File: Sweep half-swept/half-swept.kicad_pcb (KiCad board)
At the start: 2 copper layers, 109 x 86.9 mm, 25 parts, among them J2 AudioJack4dpb, SW1 SW_Push, SW10 SW_Push, SW11 SW_Push, SW12 SW_Push, SW13 SW_Push, SW14 SW_Push, SW15 SW_Push, SW16 SW_Push, SW17 SW_Push, SW2 SW_Push, SW3 SW_Push, SW4 SW_Push, SW5 SW_Push, SW6 SW_Push, SW7 SW_Push, SW8 SW_Push, SW9 SW_Push, U1 ProMicro-kbd

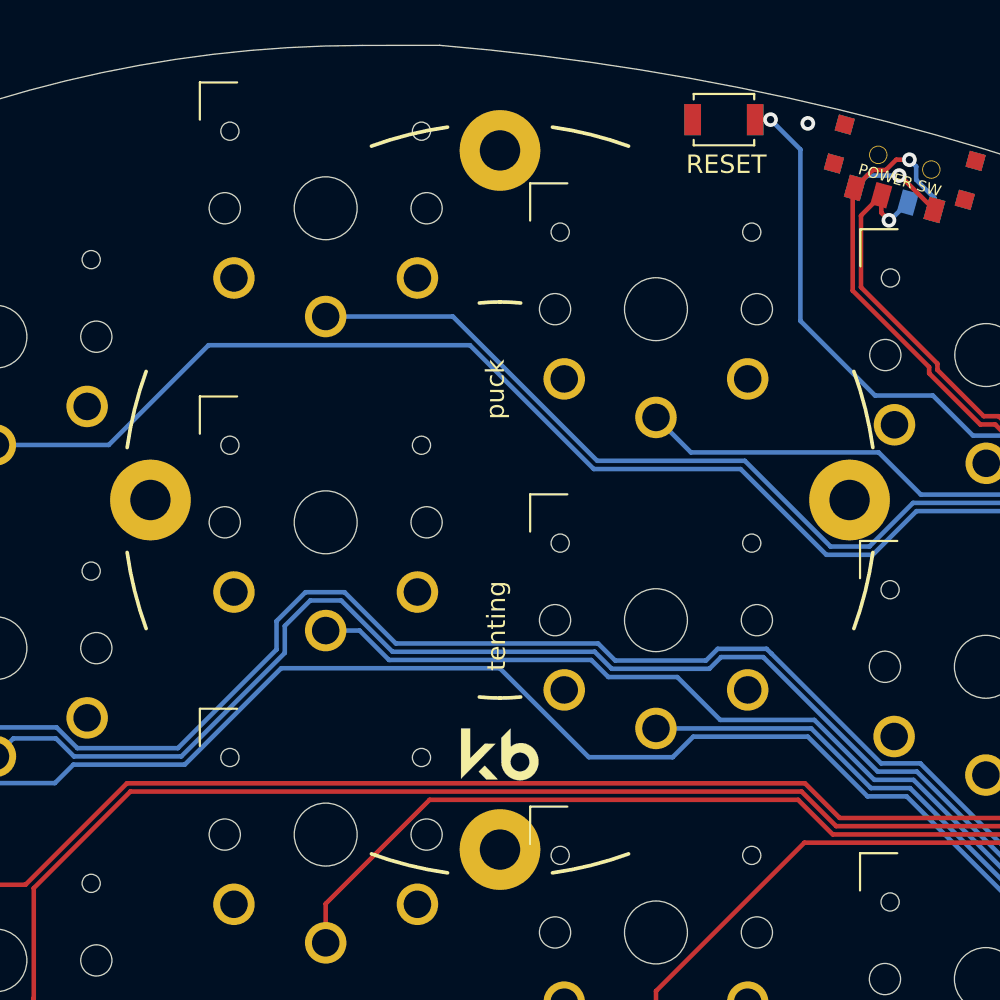
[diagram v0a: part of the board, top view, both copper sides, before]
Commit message: Remove tenting puck
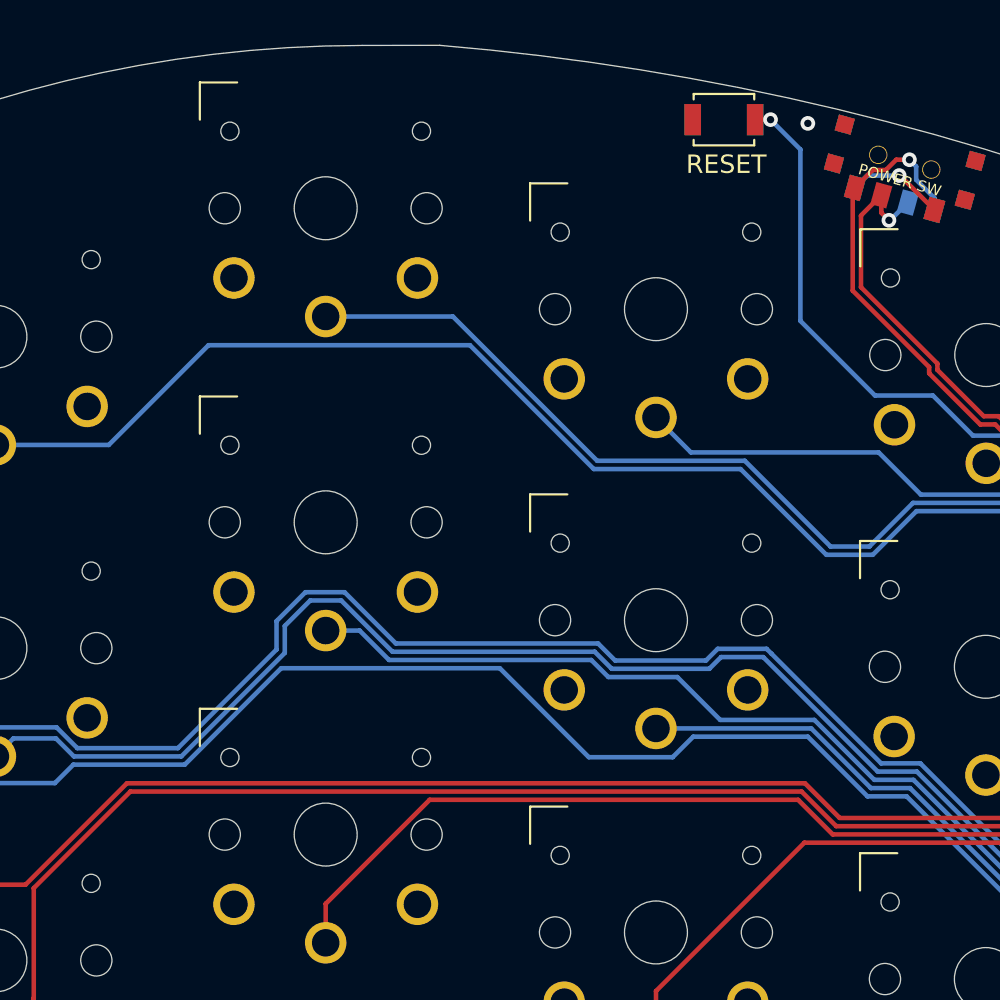
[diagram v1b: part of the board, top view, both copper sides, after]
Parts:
-  : renamed from REF**; value Tenting Puck -> (none)

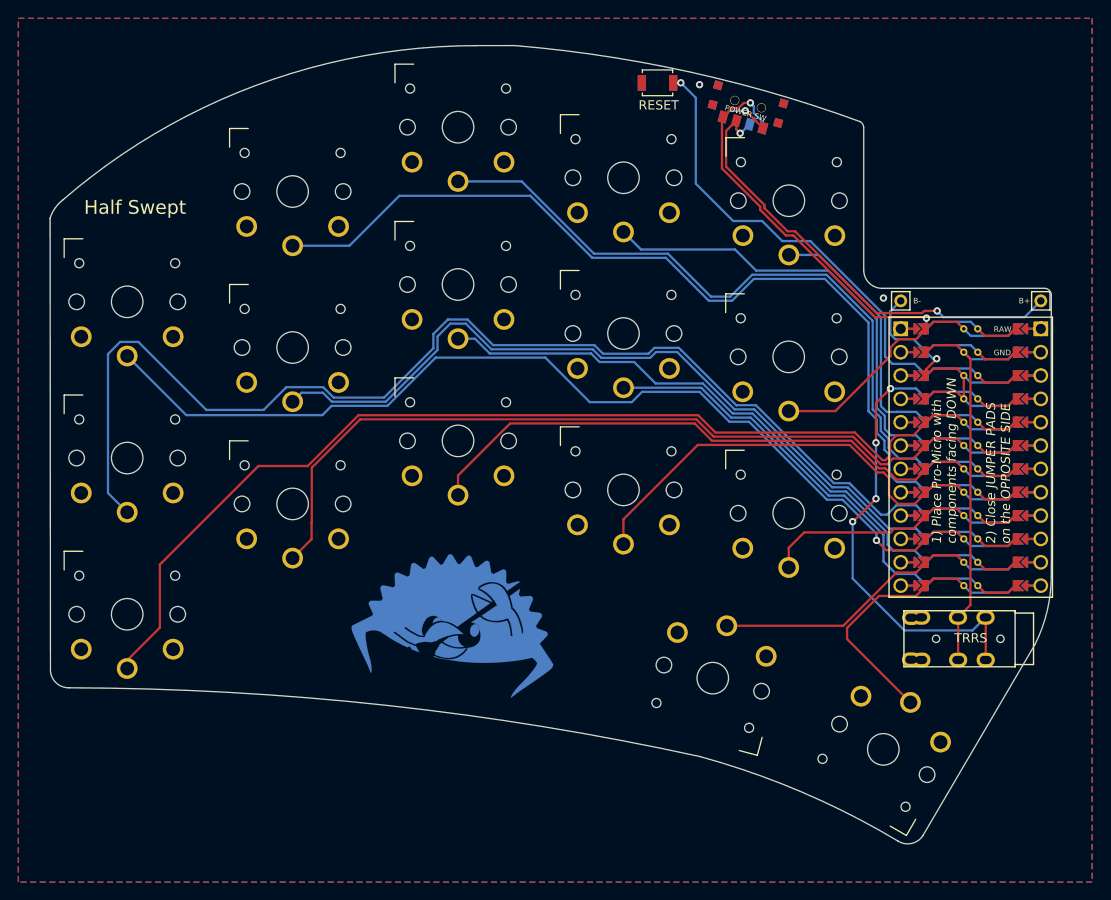
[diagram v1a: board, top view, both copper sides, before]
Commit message: Remove text from silkscreen
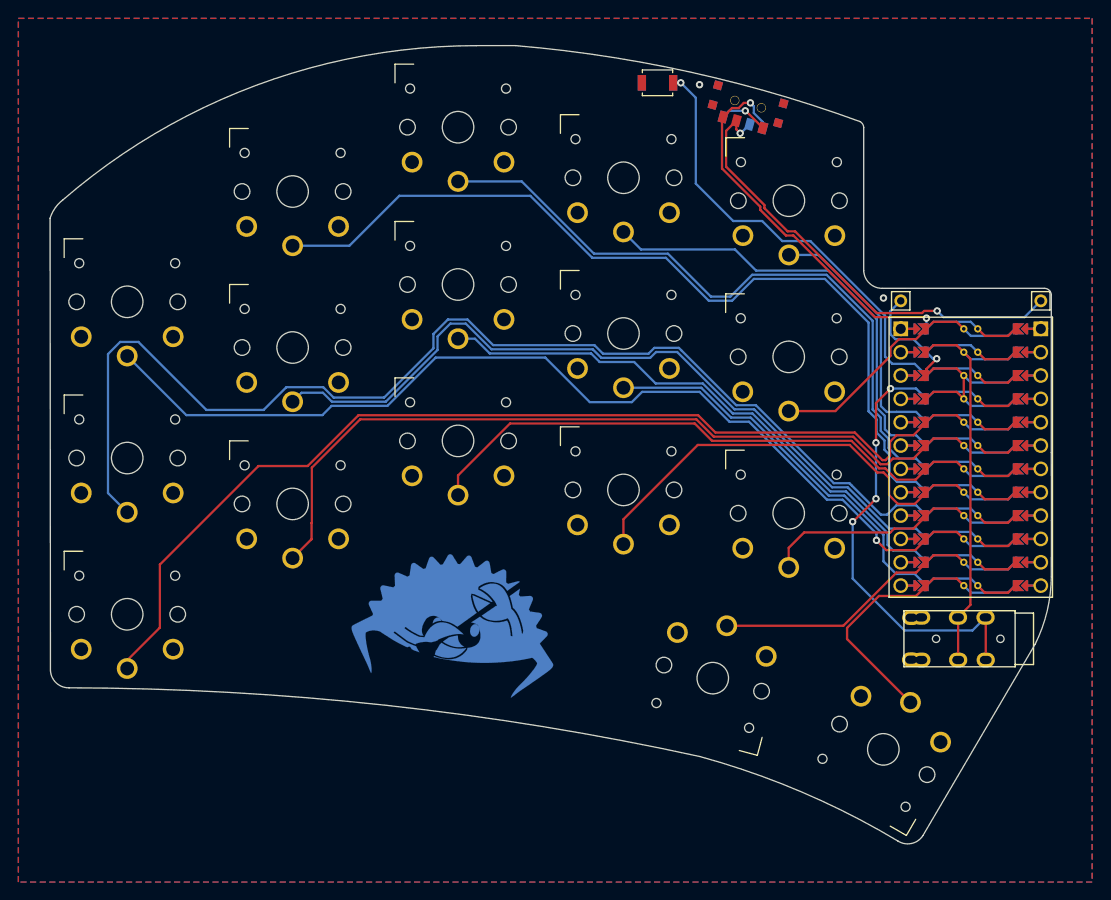
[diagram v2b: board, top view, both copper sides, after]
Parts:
-  : renamed from B+
-  : renamed from B-
-  : renamed from POWER SW
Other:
- board text removed: "1) Place Pro-Micro with components facing DOWN"
- board text removed: "2) Close JUMPER PADS on the OPPOSITE SIDE"
- board text removed: "B+"
- board text removed: "B-"
- board text removed: "GND"
- board text removed: "Half Swept"
- board text removed: "RAW"
- board text removed: "TRRS"
